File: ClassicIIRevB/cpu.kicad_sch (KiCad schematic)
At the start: 39 parts, among them U16 68030

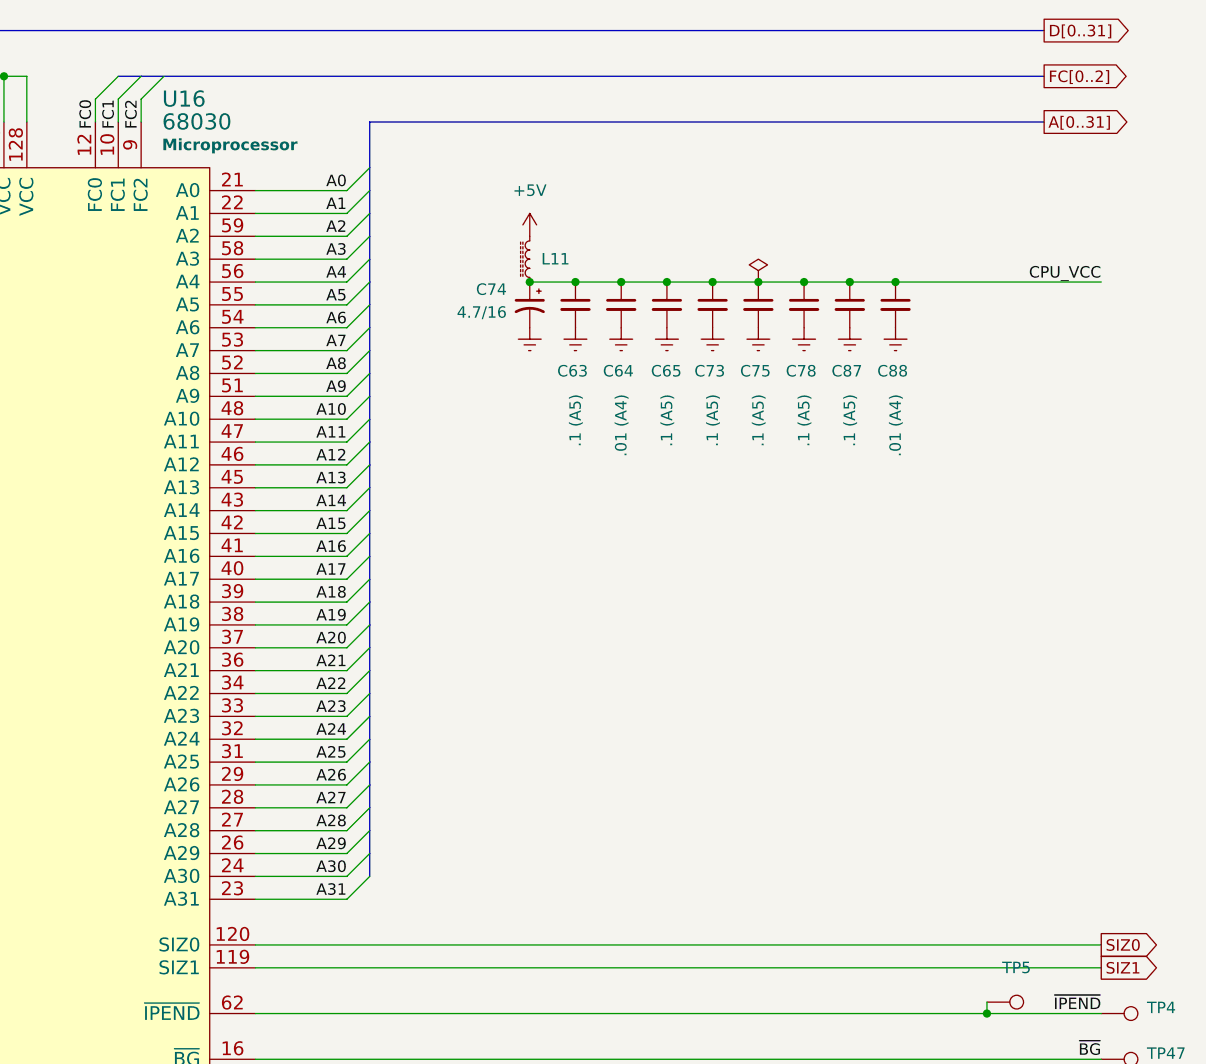
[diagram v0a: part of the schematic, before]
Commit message: Show smaller ROM footprints
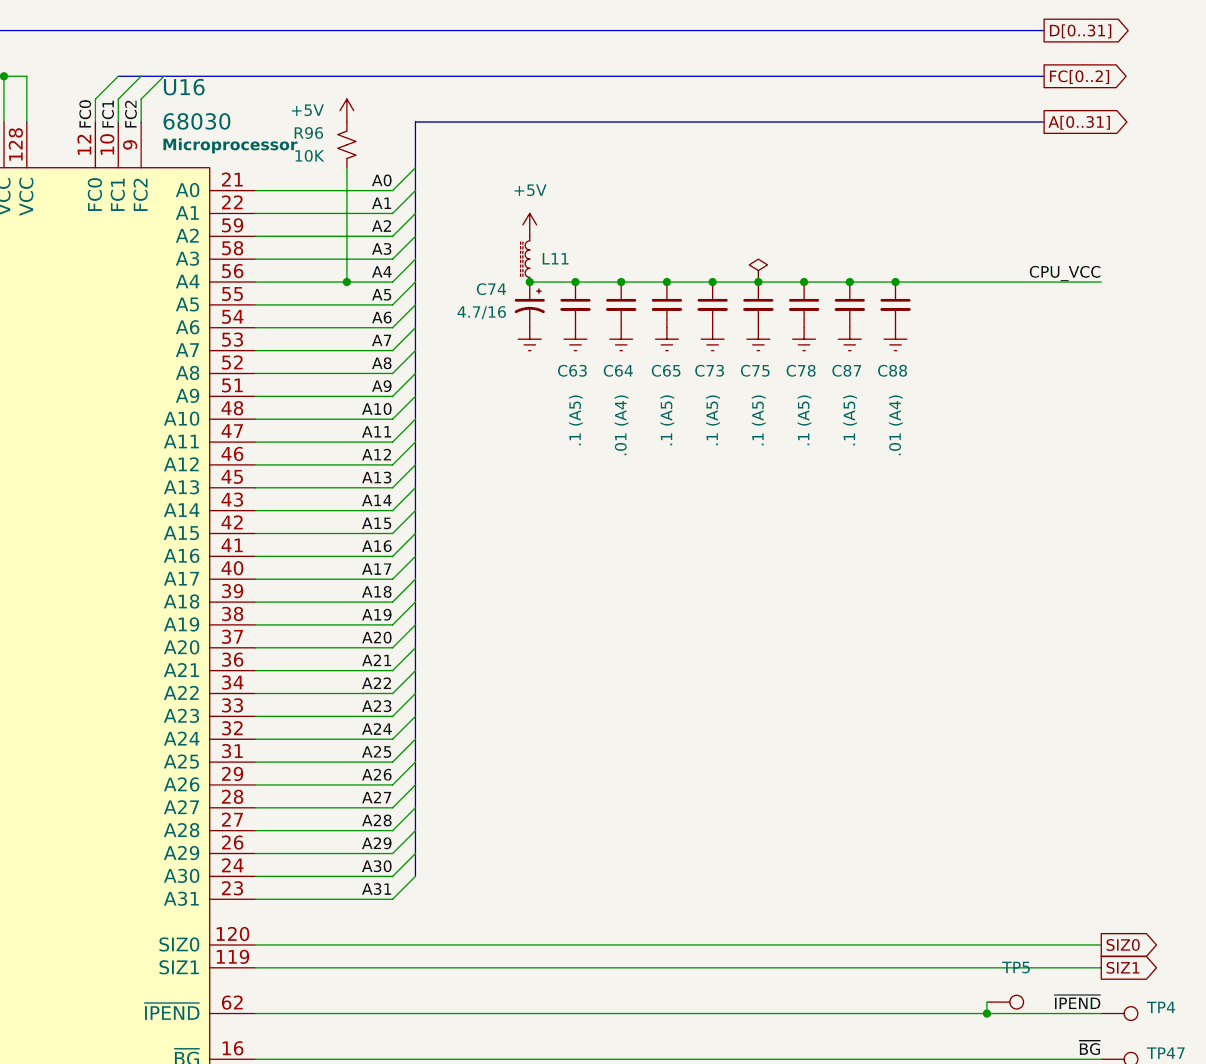
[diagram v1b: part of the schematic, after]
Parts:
- added R96: 10K, MyPackage:SMD_0805_2012Metric_Pad1.25x1.65mm, symbol Device:R_Small_US
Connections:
- net +5V: now also R96.2
- net A4: now also R96.1

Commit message: Switch to some "official" net names
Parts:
- added TP145: ~, MyPackage:TestPoint_THTPad_D1.0mm_Drill0.5mm, symbol Connector:TestPoint
- L11: value L_Ferrite_Small -> Ferrite
- renumbered TP24 to TP101, TP25 to TP117, TP26 to TP118, TP47 to TP128, TP27 to TP129, TP28 to TP130, TP4 to TP146, TP35 to TP148, TP33 to TP157, TP37 to TP158, TP46 to TP159, TP38 to TP160, TP39 to TP161, TP3 to TP169, TP2 to TP170, TP36 to TP171, TP43 to TP175, TP5 to TP255
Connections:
- net at R51.2, U16.65 (~{MMUDIS}): now also TP145.1
- net CPU_VCC renamed +5V030
- net ~{RST} renamed ~{RESET}
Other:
- moved on the sheet: C63, C64, C65, C73, C74, C75, C78, C87, C88, R41, R43, R51

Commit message: update exports
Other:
- title: Macintosh Classic II Revision B -> Macintosh Classic II (Later Revision)
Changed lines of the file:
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@@
 	(paper "USLetter")
 	(title_block
-		(title "Macintosh Classic II Revision B")
-		(date "2025-06-04")
+		(title "Macintosh Classic II (Later Revision)")
+		(date "2025-06-16")
 		(company "Apple Computer")
 		(comment 1 "drawn by Bradley Bell")

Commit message: Corrections to SMDs, more improved footprints
The later revision board reproduction design is now complete.
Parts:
- C63, C65, C73, C75, C78, C87: value .1 (A5) -> 100nF
- C64, C88: value .01 (A4) -> 10nF
- C74: value 4.7/16 -> 10uF 16V; Note (none) -> 4.7uF tant on earlier revision
- R41, R43, R47, R51, R54, R57, R64, R65, R69, R70: value 4700 -> 4.7K
- R96: value 10K -> 10K 1%
- TP101, TP117, TP118, TP128, TP129, TP130, TP145, TP146, TP148, TP157, TP158, TP159, TP160, TP161, TP169, TP170, TP171, TP175, TP255: now left out of the parts list
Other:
- moved on the sheet: R96
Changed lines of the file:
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@@
 	(title_block
 		(title "Macintosh Classic II (Later Revision)")
-		(date "2025-06-16")
+		(date "2025-06-21")
 		(company "Apple Computer")
 		(comment 1 "drawn by Bradley Bell")
@@
 	)
 	(junction
-		(at 157.48 50.8)
+		(at 154.94 50.8)
 		(diameter 0)
 		(color 0 0 0 0)
@@
 	(wire
 		(pts
-			(xy 157.48 38.1) (xy 157.48 50.8)
+			(xy 154.94 38.1) (xy 154.94 50.8)
 		)
 		(stroke
@@
 	(wire
 		(pts
+			(xy 154.94 50.8) (xy 162.56 50.8)
+		)
+		(stroke
+			(width 0)
+			(type default)
+		)
+	)
+	(wire
+		(pts
 			(xy 182.88 53.34) (xy 187.96 53.34)
 		)
@@
 	(wire
 		(pts
-			(xy 157.48 50.8) (xy 162.56 50.8)
-		)
-		(stroke
-			(width 0)
-			(type default)
-		)
-	)
-	(wire
-		(pts
 			(xy 193.04 53.34) (xy 198.12 53.34)
 		)
@@
 	(wire
 		(pts
-			(xy 147.32 50.8) (xy 157.48 50.8)
+			(xy 147.32 50.8) (xy 154.94 50.8)
 		)
 		(stroke
@@
 	(symbol
 		(lib_id "power:+5V")
-		(at 157.48 33.02 0)
+		(at 154.94 33.02 0)
 		(mirror y)
 		(unit 1)
@@
 		(fields_autoplaced yes)
 		(property "Reference" "#PWR0229"
-			(at 157.48 36.83 0)
+			(at 154.94 36.83 0)
 			(effects
 				(font
@@
 		)
 		(property "Value" "+5V"
-			(at 154.94 31.7499 0)
+			(at 157.48 31.7499 0)
 			(effects
 				(font
 					(size 1.27 1.27)
 				)
-				(justify left)
+				(justify right)
 			)
 		)
 		(property "Footprint" ""
-			(at 157.48 33.02 0)
+			(at 154.94 33.02 0)
 			(effects
 				(font
@@
 		)
 		(property "Datasheet" ""
-			(at 157.48 33.02 0)
+			(at 154.94 33.02 0)
 			(effects
 				(font
@@
 		)
 		(property "Description" "Power symbol creates a global label with name \"+5V\""
-			(at 157.48 33.02 0)
+			(at 154.94 33.02 0)
 			(effects
 				(font
@@
 			)
 		)
-		(property "Value" ".1 (A5)"
+		(property "Value" "100nF"
 			(at 208.28 68.326 90)
 			(effects
@@
 		(unit 1)
 		(exclude_from_sim no)
-		(in_bom yes)
+		(in_bom no)
 		(on_board yes)
 		(dnp no)
@@
 		(unit 1)
 		(exclude_from_sim no)
-		(in_bom yes)
+		(in_bom no)
 		(on_board yes)
 		(dnp no)
@@
 		(unit 1)
 		(exclude_from_sim no)
-		(in_bom yes)
+		(in_bom no)
 		(on_board yes)
 		(dnp no)
@@
 			)
 		)
-		(property "Value" "4700"
+		(property "Value" "4.7K"
 			(at 60.96 165.0999 0)
 			(effects
@@
 			)
 		)
-		(property "Value" "4700"
+		(property "Value" "4.7K"
 			(at 50.8 157.4799 0)
 			(effects
@@
 			)
 		)
-		(property "Value" ".1 (A5)"
+		(property "Value" "100nF"
 			(at 203.2 68.326 90)
 			(effects
@@
 	(symbol
 		(lib_id "Device:R_Small_US")
-		(at 157.48 35.56 0)
+		(at 154.94 35.56 0)
 		(mirror x)
 		(unit 1)
@@
 		(fields_autoplaced yes)
 		(property "Reference" "R96"
-			(at 154.94 34.2899 0)
+			(at 157.48 34.2899 0)
 			(effects
 				(font
 					(size 1.27 1.27)
 				)
-				(justify right)
+				(justify left)
 			)
 		)
-		(property "Value" "10K"
-			(at 154.94 36.8299 0)
+		(property "Value" "10K 1%"
+			(at 157.48 36.8299 0)
 			(effects
 				(font
 					(size 1.27 1.27)
 				)
-				(justify right)
+				(justify left)
 			)
 		)
 		(property "Footprint" "MyPackage:SMD_0805_2012Metric_Pad1.25x1.65mm"
-			(at 157.48 35.56 0)
+			(at 154.94 35.56 0)
 			(effects
 				(font
@@
 		)
 		(property "Datasheet" "~"
-			(at 157.48 35.56 0)
+			(at 154.94 35.56 0)
 			(effects
 				(font
@@
 		)
 		(property "Description" "Resistor, small US symbol"
-			(at 157.48 35.56 0)
+			(at 154.94 35.56 0)
 			(effects
 				(font
@@
 		(unit 1)
 		(exclude_from_sim no)
-		(in_bom yes)
+		(in_bom no)
 		(on_board yes)
 		(dnp no)
@@
 		(unit 1)
 		(exclude_from_sim no)
-		(in_bom yes)
+		(in_bom no)
 		(on_board yes)
 		(dnp no)
@@
 		(unit 1)
 		(exclude_from_sim no)
-		(in_bom yes)
+		(in_bom no)
 		(on_board yes)
 		(dnp no)
@@
 		(unit 1)
 		(exclude_from_sim no)
-		(in_bom yes)
+		(in_bom no)
 		(on_board yes)
 		(dnp no)
@@
 		(fields_autoplaced yes)
 		(property "Reference" "U16"
-			(at 136.9379 29.21 0)
+			(at 136.9379 30.48 0)
 			(effects
 				(font
-					(size 1.778 1.778)
+					(size 1.27 1.27)
 				)
 				(justify left)
@@
 			(effects
 				(font
-					(size 1.778 1.778)
+					(size 1.27 1.27)
 				)
 				(justify left)
@@
 		(unit 1)
 		(exclude_from_sim no)
-		(in_bom yes)
+		(in_bom no)
 		(on_board yes)
 		(dnp no)
@@
 		(unit 1)
 		(exclude_from_sim no)
-		(in_bom yes)
+		(in_bom no)
 		(on_board yes)
 		(dnp no)
@@
 		(unit 1)
 		(exclude_from_sim no)
-		(in_bom yes)
+		(in_bom no)
 		(on_board yes)
 		(dnp no)
@@
 		(unit 1)
 		(exclude_from_sim no)
-		(in_bom yes)
+		(in_bom no)
 		(on_board yes)
 		(dnp no)
@@
 			)
 		)
-		(property "Value" "4700"
+		(property "Value" "4.7K"
 			(at 50.8 144.7799 0)
 			(effects
@@
 			)
 		)
-		(property "Value" ".1 (A5)"
+		(property "Value" "100nF"
 			(at 198.12 68.326 90)
 			(effects
@@
 		(unit 1)
 		(exclude_from_sim no)
-		(in_bom yes)
+		(in_bom no)
 		(on_board yes)
 		(dnp no)
@@
 			)
 		)
-		(property "Value" "4700"
+		(property "Value" "4.7K"
 			(at 48.26 134.6199 0)
 			(effects
@@
 		(unit 1)
 		(exclude_from_sim no)
-		(in_bom yes)
+		(in_bom no)
 		(on_board yes)
 		(dnp no)
@@
 		(unit 1)
 		(exclude_from_sim no)
-		(in_bom yes)
+		(in_bom no)
 		(on_board yes)
 		(dnp no)
@@
 			)
 		)
-		(property "Value" ".1 (A5)"
+		(property "Value" "100nF"
 			(at 193.04 68.326 90)
 			(do_not_autoplace yes)
@@
 			)
 		)
-		(property "Value" ".01 (A4)"
+		(property "Value" "10nF"
 			(at 187.96 68.326 90)
 			(effects
@@
 		(unit 1)
 		(exclude_from_sim no)
-		(in_bom yes)
+		(in_bom no)
 		(on_board yes)
 		(dnp no)
@@
 		(unit 1)
 		(exclude_from_sim no)
-		(in_bom yes)
+		(in_bom no)
 		(on_board yes)
 		(dnp no)
@@
 			)
 		)
-		(property "Value" ".1 (A5)"
+		(property "Value" "100nF"
 			(at 213.36 68.326 90)
 			(effects
@@
 			)
 		)
-		(property "Value" ".01 (A4)"
+		(property "Value" "10nF"
 			(at 218.44 68.326 90)
 			(effects
@@
 			)
 		)
-		(property "Value" "4700"
+		(property "Value" "4.7K"
 			(at 50.8 167.6399 0)
 			(effects
@@
 			)
 		)
-		(property "Value" "4700"
+		(property "Value" "4.7K"
 			(at 154.94 149.8599 0)
 			(effects
@@
 		(on_board yes)
 		(dnp no)
-		(fields_autoplaced yes)
 		(property "Reference" "C74"
-			(at 175.26 56.7181 0)
+			(at 177.038 53.848 0)
 			(effects
 				(font
@@
 			)
 		)
-		(property "Value" "4.7/16"
-			(at 175.26 59.2581 0)
+		(property "Value" "10uF 16V"
+			(at 177.038 56.388 0)
 			(effects
 				(font
@@
 			)
 		)
+		(property "Note" "4.7uF tant on earlier revision"
+			(at 174.752 57.658 90)
+			(effects
+				(font
+					(size 1.27 1.27)
+				)
+				(justify right)
+			)
+		)
 		(pin "2"
 		)
@@
 		(unit 1)
 		(exclude_from_sim no)
-		(in_bom yes)
+		(in_bom no)
 		(on_board yes)
 		(dnp no)
@@
 			)
 		)
-		(property "Value" "4700"
+		(property "Value" "4.7K"
 			(at 58.42 134.6199 0)
 			(effects
@@
 		(unit 1)
 		(exclude_from_sim no)
-		(in_bom yes)
+		(in_bom no)
 		(on_board yes)
 		(dnp no)
@@
 			)
 		)
-		(property "Value" "4700"
+		(property "Value" "4.7K"
 			(at 48.26 175.2599 0)
 			(effects
@@
 			)
 		)
-		(property "Value" "4700"
+		(property "Value" "4.7K"
 			(at 165.1 160.0199 0)
 			(effects
@@
 			)
 		)
-		(property "Value" "4700"
+		(property "Value" "4.7K"
 			(at 58.42 172.7199 0)
 			(effects
@@
 			)
 		)
-		(property "Value" ".1 (A5)"
+		(property "Value" "100nF"
 			(at 182.88 68.326 90)
 			(effects
@@
 		(unit 1)
 		(exclude_from_sim no)
-		(in_bom yes)
+		(in_bom no)
 		(on_board yes)
 		(dnp no)
